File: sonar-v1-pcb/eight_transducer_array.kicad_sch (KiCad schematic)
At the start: 22 parts, among them U201 ADS8568SPM

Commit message: WIP hand-off: rx amp sim project, SPICE models, schematic updates
Adds rx_amp_sim KiCad project, SPICE models, Python setup-kicad.py
(replaces test_py.sh), CLAUDE.md, and a sweep of schematic edits across
the v1 board.

Co-Authored-By: Claude Opus 4.7 <noreply@anthropic.com>
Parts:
- renumbered C203 to C10, C204 to C11, C213 to C12, C205 to C13, C210 to C14, C206 to C15, C207 to C16, C208 to C17, C209 to C18, C214 to C19, C201 to C4, C211 to C5, C215 to C6, C202 to C7, C212 to C8, C216 to C9, R201 to R3, R202 to R4, R204 to R5, R203 to R6, R205 to R7, U201 to U2

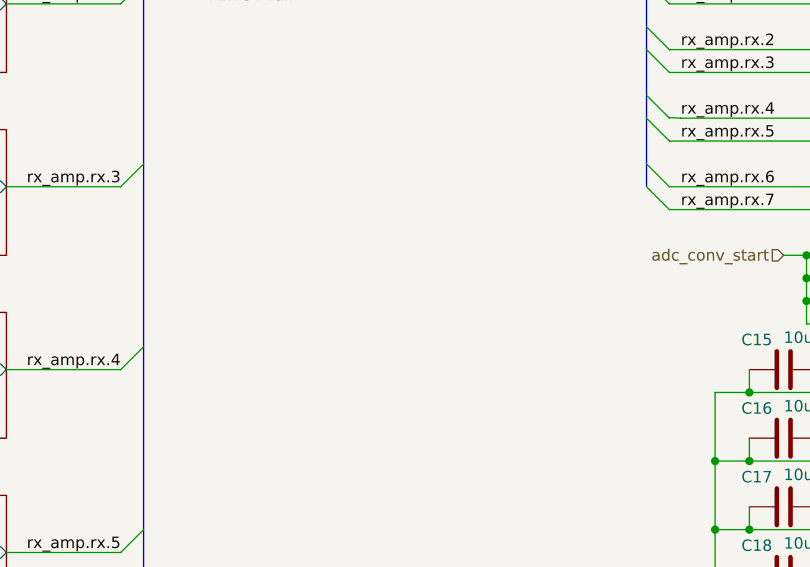
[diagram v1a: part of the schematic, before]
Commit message: Add quad RX pre-amp and MEMS RX sheets; RX amp rework
- New sub-sheets quad_rx_pre_amp and mems_rx added under the
  eight_transducer_array, with R_GAIN_HIGH/R_GAIN_TARGET project
  text variables to parameterize gain
- Substantial rework of rx_amp.kicad_sch
- rx_amp_sim: add OP analysis to the workbook
- Drop stale sonar.csv export
- Add .gitignore for KiCad user-local files (*.kicad_prl, ~*.lck,
  *-backups/, *.bak, fp-info-cache) and VS Code .history/

Co-Authored-By: Claude Opus 4.7 <noreply@anthropic.com>
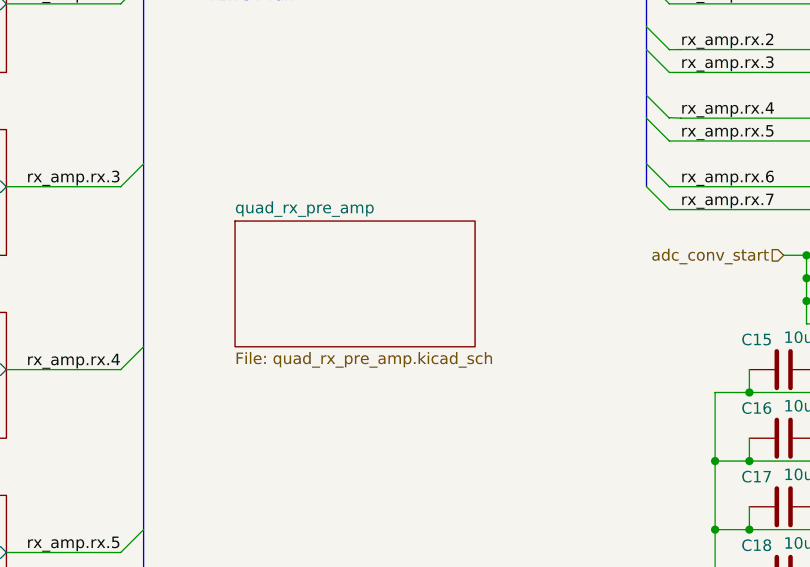
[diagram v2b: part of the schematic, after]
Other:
- added sheet quad_rx_pre_amp (quad_rx_pre_amp.kicad_sch)
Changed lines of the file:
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@@
+	)
+	(sheet
+		(at 71.12 91.44)
+		(size 26.67 13.97)
+		(exclude_from_sim no)
+		(in_bom yes)
+		(on_board yes)
+		(dnp no)
+		(fields_autoplaced yes)
+		(stroke
+			(width 0.1524)
+			(type solid)
+		)
+		(fill
+			(color 0 0 0 0)
+		)
+		(property "Sheetname" "quad_rx_pre_amp"
+			(at 71.12 90.7284 0)
+			(show_name no)
+			(do_not_autoplace no)
+			(effects
+				(font
+					(size 1.27 1.27)
+				)
+				(justify left bottom)
+			)
+		)
+		(property "Sheetfile" "quad_rx_pre_amp.kicad_sch"
+			(at 71.12 105.9946 0)
+			(show_name no)
+			(do_not_autoplace no)
+			(effects
+				(font
+					(size 1.27 1.27)
+				)
+				(justify left top)
+			)
+		)
+		(instances
+			(project "sonar"
+				(path "/f72ceae0-eee4-4385-b0e8-639846bcb5f2/d78844ef-eb5d-4b24-a5c3-8824db20c2bc"
+					(page "40")
+				)
+			)
+		)
 	)
 	(sheet
